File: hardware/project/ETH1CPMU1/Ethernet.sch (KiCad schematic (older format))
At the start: 43 parts, among them U401 LC03-3.3, U402 LAN8742A, U403 LC03-3.3, Y401 NX5032GA-25.000M-LN-CD-1

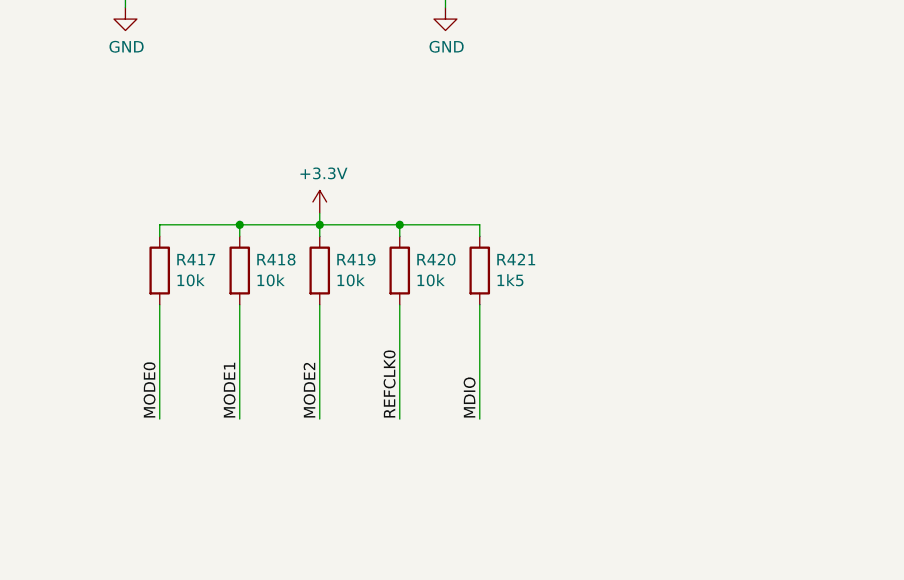
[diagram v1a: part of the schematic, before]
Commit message: Function generator schematic design.
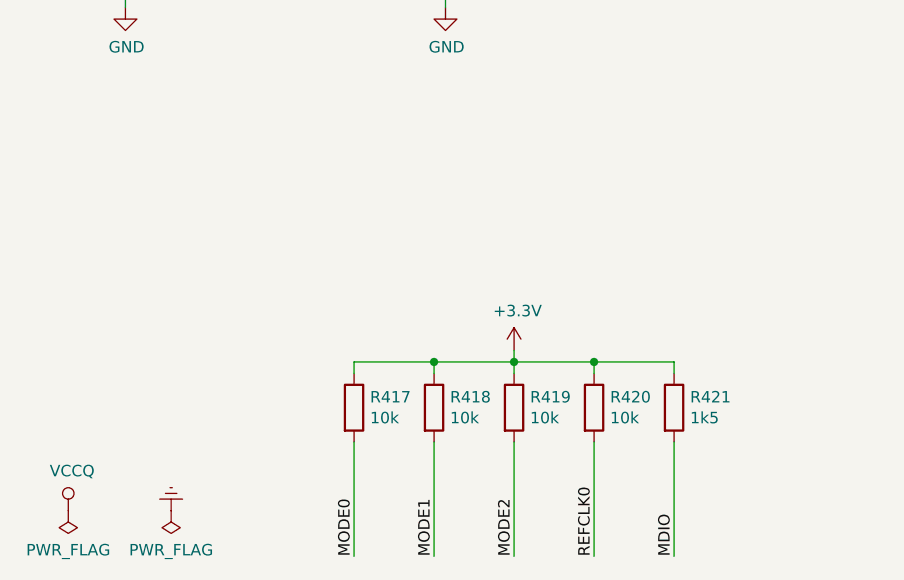
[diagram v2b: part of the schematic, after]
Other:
- moved on the sheet: R417, R418, R419, R420, R421
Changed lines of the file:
@@
 $Descr A4 11693 8268
 encoding utf-8
-Sheet 3 14
+Sheet 4 15
 Title "Ethernet"
 Date ""
@@
 L Device:R R417
 U 1 1 5D90AA6A
-P 1350 6300
-F 0 "R417" H 1420 6346 50  0000 L CNN
-F 1 "10k" H 1420 6255 50  0000 L CNN
-F 2 "Resistor_SMD:R_0603_1608Metric_Pad1.05x0.95mm_HandSolder" V 1280 6300 50  0001 C CNN
-F 3 "~" H 1350 6300 50  0001 C CNN
-	1    1350 6300
+P 2200 6900
+F 0 "R417" H 2270 6946 50  0000 L CNN
+F 1 "10k" H 2270 6855 50  0000 L CNN
+F 2 "Resistor_SMD:R_0603_1608Metric_Pad1.05x0.95mm_HandSolder" V 2130 6900 50  0001 C CNN
+F 3 "~" H 2200 6900 50  0001 C CNN
+	1    2200 6900
 	1    0    0    -1
 $EndComp
@@
 L Device:R R418
 U 1 1 5D90BF82
-P 1700 6300
-F 0 "R418" H 1770 6346 50  0000 L CNN
-F 1 "10k" H 1770 6255 50  0000 L CNN
-F 2 "Resistor_SMD:R_0603_1608Metric_Pad1.05x0.95mm_HandSolder" V 1630 6300 50  0001 C CNN
-F 3 "~" H 1700 6300 50  0001 C CNN
-	1    1700 6300
+P 2550 6900
+F 0 "R418" H 2620 6946 50  0000 L CNN
+F 1 "10k" H 2620 6855 50  0000 L CNN
+F 2 "Resistor_SMD:R_0603_1608Metric_Pad1.05x0.95mm_HandSolder" V 2480 6900 50  0001 C CNN
+F 3 "~" H 2550 6900 50  0001 C CNN
+	1    2550 6900
 	1    0    0    -1
 $EndComp
@@
 L Device:R R419
 U 1 1 5D90C23E
-P 2050 6300
-F 0 "R419" H 2120 6346 50  0000 L CNN
-F 1 "10k" H 2120 6255 50  0000 L CNN
-F 2 "Resistor_SMD:R_0603_1608Metric_Pad1.05x0.95mm_HandSolder" V 1980 6300 50  0001 C CNN
-F 3 "~" H 2050 6300 50  0001 C CNN
-	1    2050 6300
-	1    0    0    -1
-$EndComp
-Wire Wire Line
-	1350 6150 1350 6100
-Wire Wire Line
-	1350 6100 1700 6100
-Wire Wire Line
-	2050 6100 2050 6150
-Wire Wire Line
-	1700 6150 1700 6100
-Connection ~ 1700 6100
-Wire Wire Line
-	1700 6100 2050 6100
-Wire Wire Line
-	1350 6450 1350 6950
-Wire Wire Line
-	1700 6450 1700 6950
-Wire Wire Line
-	2050 6450 2050 6950
+P 2900 6900
+F 0 "R419" H 2970 6946 50  0000 L CNN
+F 1 "10k" H 2970 6855 50  0000 L CNN
+F 2 "Resistor_SMD:R_0603_1608Metric_Pad1.05x0.95mm_HandSolder" V 2830 6900 50  0001 C CNN
+F 3 "~" H 2900 6900 50  0001 C CNN
+	1    2900 6900
+	1    0    0    -1
+$EndComp
+Wire Wire Line
+	2200 6750 2200 6700
+Wire Wire Line
+	2200 6700 2550 6700
+Wire Wire Line
+	2900 6700 2900 6750
+Wire Wire Line
+	2550 6750 2550 6700
+Connection ~ 2550 6700
+Wire Wire Line
+	2550 6700 2900 6700
+Wire Wire Line
+	2200 7050 2200 7550
+Wire Wire Line
+	2550 7050 2550 7550
+Wire Wire Line
+	2900 7050 2900 7550
 Text Label 4600 2900 2    50   ~ 0
 ETH_TXP
@@
 Connection ~ 2200 1050
 Wire Wire Line
-	2050 6050 2050 6100
+	2900 6650 2900 6700
 Wire Notes Line
 	8350 6450 8350 5100
@@
 L power:+3.3V #PWR0421
 U 1 1 5DACAFF6
-P 2050 6050
-F 0 "#PWR0421" H 2050 5900 50  0001 C CNN
-F 1 "+3.3V" H 2065 6223 50  0000 C CNN
-F 2 "" H 2050 6050 50  0001 C CNN
-F 3 "" H 2050 6050 50  0001 C CNN
-	1    2050 6050
+P 2900 6650
+F 0 "#PWR0421" H 2900 6500 50  0001 C CNN
+F 1 "+3.3V" H 2915 6823 50  0000 C CNN
+F 2 "" H 2900 6650 50  0001 C CNN
+F 3 "" H 2900 6650 50  0001 C CNN
+	1    2900 6650
 	1    0    0    -1
 $EndComp
@@
 Text Label 2350 3400 0    50   ~ 0
 MODE2
-Text Label 1350 6950 1    50   ~ 0
+Text Label 2200 7550 1    50   ~ 0
 MODE0
-Text Label 1700 6950 1    50   ~ 0
+Text Label 2550 7550 1    50   ~ 0
 MODE1
 Text Label 2350 3500 0    50   ~ 0
 MDIO
-Text Label 2050 6950 1    50   ~ 0
+Text Label 2900 7550 1    50   ~ 0
 MODE2
 $Comp
 L Device:R R420
 U 1 1 5DA59190
-P 2400 6300
-F 0 "R420" H 2470 6346 50  0000 L CNN
-F 1 "10k" H 2470 6255 50  0000 L CNN
-F 2 "Resistor_SMD:R_0603_1608Metric_Pad1.05x0.95mm_HandSolder" V 2330 6300 50  0001 C CNN
-F 3 "~" H 2400 6300 50  0001 C CNN
-	1    2400 6300
-	1    0    0    -1
-$EndComp
-Wire Wire Line
-	2400 6150 2400 6100
-Wire Wire Line
-	2400 6100 2050 6100
-Connection ~ 2050 6100
-Wire Wire Line
-	2400 6450 2400 6950
-Text Label 2400 6950 1    50   ~ 0
+P 3250 6900
+F 0 "R420" H 3320 6946 50  0000 L CNN
+F 1 "10k" H 3320 6855 50  0000 L CNN
+F 2 "Resistor_SMD:R_0603_1608Metric_Pad1.05x0.95mm_HandSolder" V 3180 6900 50  0001 C CNN
+F 3 "~" H 3250 6900 50  0001 C CNN
+	1    3250 6900
+	1    0    0    -1
+$EndComp
+Wire Wire Line
+	3250 6750 3250 6700
+Wire Wire Line
+	3250 6700 2900 6700
+Connection ~ 2900 6700
+Wire Wire Line
+	3250 7050 3250 7550
+Text Label 3250 7550 1    50   ~ 0
 REFCLK0
 $Comp
 L Device:R R421
 U 1 1 5DA75FC2
-P 2750 6300
-F 0 "R421" H 2820 6346 50  0000 L CNN
-F 1 "1k5" H 2820 6255 50  0000 L CNN
-F 2 "Resistor_SMD:R_0603_1608Metric_Pad1.05x0.95mm_HandSolder" V 2680 6300 50  0001 C CNN
-F 3 "~" H 2750 6300 50  0001 C CNN
-	1    2750 6300
-	1    0    0    -1
-$EndComp
-Wire Wire Line
-	2750 6150 2750 6100
-Wire Wire Line
-	2750 6100 2400 6100
-Connection ~ 2400 6100
-Wire Wire Line
-	2750 6450 2750 6950
-Text Label 2750 6950 1    50   ~ 0
+P 3600 6900
+F 0 "R421" H 3670 6946 50  0000 L CNN
+F 1 "1k5" H 3670 6855 50  0000 L CNN
+F 2 "Resistor_SMD:R_0603_1608Metric_Pad1.05x0.95mm_HandSolder" V 3530 6900 50  0001 C CNN
+F 3 "~" H 3600 6900 50  0001 C CNN
+	1    3600 6900
+	1    0    0    -1
+$EndComp
+Wire Wire Line
+	3600 6750 3600 6700
+Wire Wire Line
+	3600 6700 3250 6700
+Connection ~ 3250 6700
+Wire Wire Line
+	3600 7050 3600 7550
+Text Label 3600 7550 1    50   ~ 0
 MDIO
 $Comp
@@
 Wire Wire Line
 	5700 2900 7950 2900
+$Comp
+L power:VCCQ #PWR0422
+U 1 1 5DD7CA2A
+P 950 7350
+F 0 "#PWR0422" H 950 7200 50  0001 C CNN
+F 1 "VCCQ" H 967 7523 50  0000 C CNN
+F 2 "" H 950 7350 50  0001 C CNN
+F 3 "" H 950 7350 50  0001 C CNN
+	1    950  7350
+	1    0    0    -1
+$EndComp
+$Comp
+L power:PWR_FLAG #FLG0403
+U 1 1 5DD89006
+P 950 7350
+F 0 "#FLG0403" H 950 7425 50  0001 C CNN
+F 1 "PWR_FLAG" H 950 7523 50  0000 C CNN
+F 2 "" H 950 7350 50  0001 C CNN
+F 3 "~" H 950 7350 50  0001 C CNN
+	1    950  7350
+	-1   0    0    1
+$EndComp
+$Comp
+L power:Earth #PWR0423
+U 1 1 5DDA24E1
+P 1400 7350
+F 0 "#PWR0423" H 1400 7100 50  0001 C CNN
+F 1 "Earth" H 1400 7200 50  0001 C CNN
+F 2 "" H 1400 7350 50  0001 C CNN
+F 3 "~" H 1400 7350 50  0001 C CNN
+	1    1400 7350
+	-1   0    0    1
+$EndComp
+$Comp
+L power:PWR_FLAG #FLG0404
+U 1 1 5DDAD668
+P 1400 7350
+F 0 "#FLG0404" H 1400 7425 50  0001 C CNN
+F 1 "PWR_FLAG" H 1400 7523 50  0000 C CNN
+F 2 "" H 1400 7350 50  0001 C CNN
+F 3 "~" H 1400 7350 50  0001 C CNN
+	1    1400 7350
+	-1   0    0    1
+$EndComp
 $EndSCHEMATC

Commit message: New footprint development, changes in schematics.
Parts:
- FB401: footprint Resistor_SMD:R_0805_2012Metric_Pad1.15x1.40mm_HandSolder -> Inductor_SMD:L_0805_2012Metric_Pad1.15x1.40mm_HandSolder
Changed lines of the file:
@@
 F 0 "FB401" V 3226 1050 50  0000 C CNN
 F 1 "742792031" V 3317 1050 50  0000 C CNN
-F 2 "Resistor_SMD:R_0805_2012Metric_Pad1.15x1.40mm_HandSolder" V 3430 1050 50  0001 C CNN
+F 2 "Inductor_SMD:L_0805_2012Metric_Pad1.15x1.40mm_HandSolder" V 3430 1050 50  0001 C CNN
 F 3 "~" H 3500 1050 50  0001 C CNN
 	1    3500 1050

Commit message: Schematic and PCB design.
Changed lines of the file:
@@
 	2450 2150 2650 2150
 $Comp
-L power:PWR_FLAG #FLG0402
+L power:PWR_FLAG #FLG0401
 U 1 1 5D788385
 P 2100 1750
-F 0 "#FLG0402" H 2100 1825 50  0001 C CNN
+F 0 "#FLG0401" H 2100 1825 50  0001 C CNN
 F 1 "PWR_FLAG" V 2100 1877 50  0000 L CNN
 F 2 "" H 2100 1750 50  0001 C CNN
@@
 $EndComp
 Connection ~ 5050 1050
-$Comp
-L power:PWR_FLAG #FLG0401
-U 1 1 5D82F1E4
-P 5050 1000
-F 0 "#FLG0401" H 5050 1075 50  0001 C CNN
-F 1 "PWR_FLAG" H 5050 1173 50  0000 C CNN
-F 2 "" H 5050 1000 50  0001 C CNN
-F 3 "~" H 5050 1000 50  0001 C CNN
-	1    5050 1000
-	1    0    0    -1
-$EndComp
-Wire Wire Line
-	5050 1000 5050 1050
 Wire Wire Line
 	5250 1100 5250 1050
@@
 $EndComp
 $Comp
-L power:PWR_FLAG #FLG0403
+L power:PWR_FLAG #FLG0402
 U 1 1 5DD89006
 P 950 7350
-F 0 "#FLG0403" H 950 7425 50  0001 C CNN
+F 0 "#FLG0402" H 950 7425 50  0001 C CNN
 F 1 "PWR_FLAG" H 950 7523 50  0000 C CNN
 F 2 "" H 950 7350 50  0001 C CNN
@@
 $EndComp
 $Comp
-L power:PWR_FLAG #FLG0404
+L power:PWR_FLAG #FLG0403
 U 1 1 5DDAD668
 P 1400 7350
-F 0 "#FLG0404" H 1400 7425 50  0001 C CNN
+F 0 "#FLG0403" H 1400 7425 50  0001 C CNN
 F 1 "PWR_FLAG" H 1400 7523 50  0000 C CNN
 F 2 "" H 1400 7350 50  0001 C CNN

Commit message: PCB design.
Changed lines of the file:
@@
 U 1 1 5D77A84D
 P 4400 3500
-F 0 "R409" V 4300 3500 50  0000 C CNN
-F 1 "12k1" V 4400 3500 50  0000 C CNN
+F 0 "R409" V 4200 3500 50  0000 C CNN
+F 1 "12k1" V 4300 3500 50  0000 C CNN
 F 2 "Resistor_SMD:R_0603_1608Metric_Pad1.05x0.95mm_HandSolder" V 4330 3500 50  0001 C CNN
 F 3 "~" H 4400 3500 50  0001 C CNN

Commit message: PCB design
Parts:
- renumbered C413 to C401, C401 to C402, C408 to C403, C414 to C404, C402 to C405, C409 to C406, C403 to C407, C404 to C408, C405 to C409, C406 to C410, C407 to C411, C410 to C412, C412 to C413, C411 to C414, R405 to R401, R406 to R402, R407 to R403, R408 to R404, R412 to R405, R417 to R406, R418 to R407, R419 to R408, R420 to R409, R421 to R410, R413 to R411, R409 to R412, R414 to R413, R415 to R414, R401 to R415, R402 to R416, R403 to R417, R404 to R418, R416 to R419, R410 to R420, R411 to R421, U402 to U401, U401 to U402
